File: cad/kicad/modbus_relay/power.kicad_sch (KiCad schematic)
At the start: 18 parts, among them Q6 AO3401A, U3 LMR33630ADDA

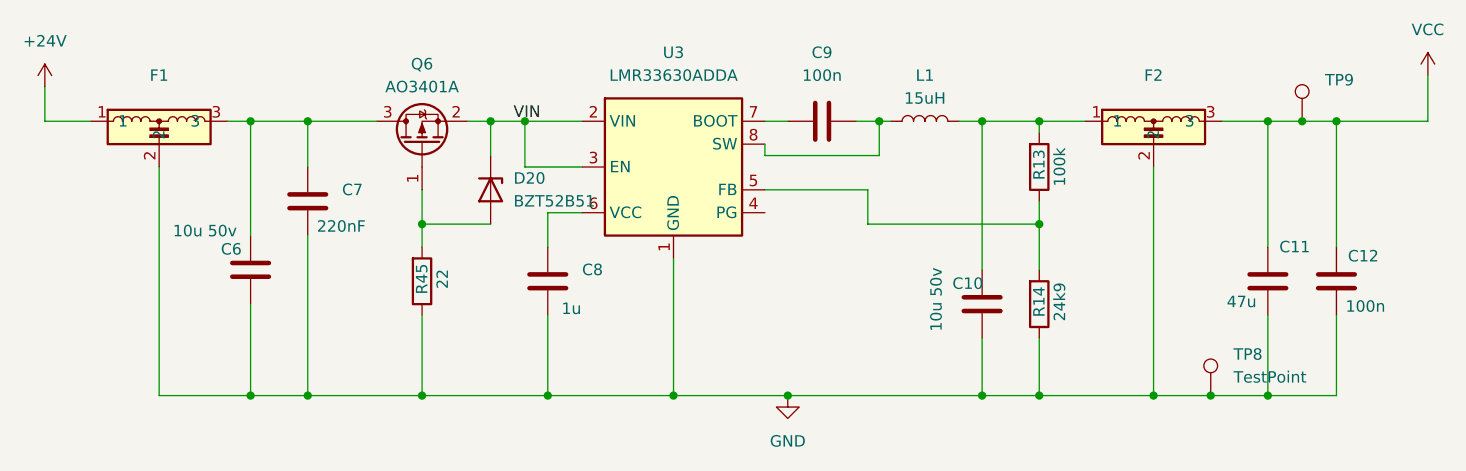
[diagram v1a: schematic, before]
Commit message: Double sided version
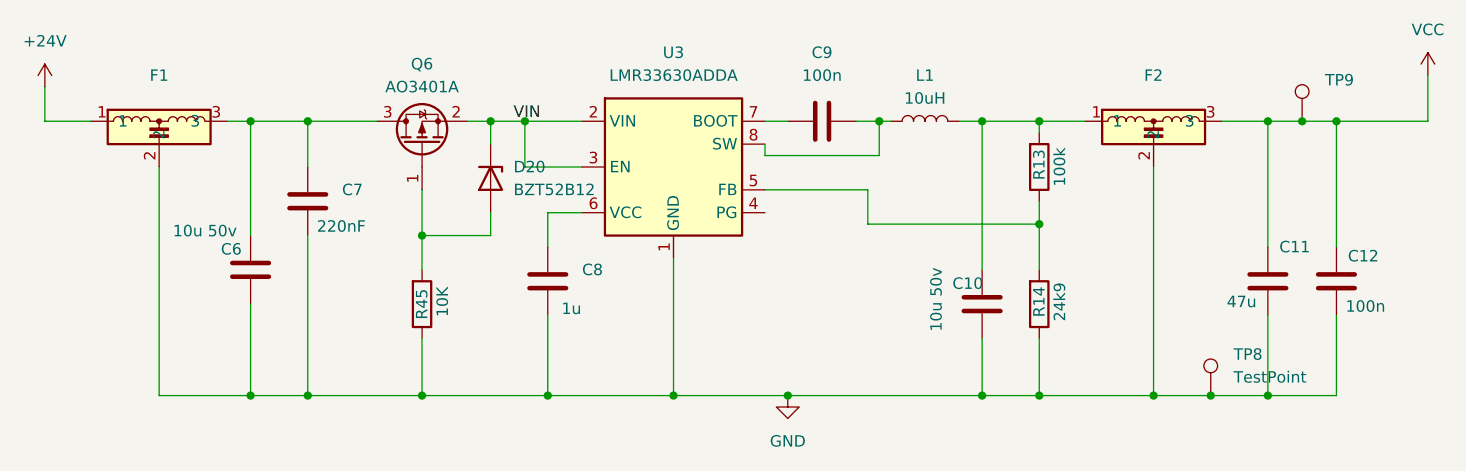
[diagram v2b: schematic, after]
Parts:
- C12: footprint Capacitor_SMD:C_0603_1608Metric_Pad1.08x0.95mm_HandSolder -> Capacitor_SMD:C_0805_2012Metric_Pad1.18x1.45mm_HandSolder
- D20: value BZT52B51 -> BZT52B12
- L1: value 15uH -> 10uH; footprint Inductor_SMD:L_Wuerth_HCM-7070 -> Inductor_SMD:L_Bourns_SRP6060FA
- R13, R14: footprint Resistor_SMD:R_0603_1608Metric_Pad0.98x0.95mm_HandSolder -> Resistor_SMD:R_0805_2012Metric_Pad1.20x1.40mm_HandSolder
- R45: value 22 -> 10K; footprint Resistor_SMD:R_0603_1608Metric_Pad0.98x0.95mm_HandSolder -> Resistor_SMD:R_0805_2012Metric_Pad1.20x1.40mm_HandSolder
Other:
- moved on the sheet: D20, R45
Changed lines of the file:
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@@
-	)
-	(junction
-		(at 107.95 92.71)
-		(diameter 0)
-		(color 0 0 0 0)
 	)
 	(junction
@@
 	)
 	(junction
+		(at 107.95 93.98)
+		(diameter 0)
+		(color 0 0 0 0)
+	)
+	(junction
 		(at 201.93 81.28)
 		(diameter 0)
@@
 	(wire
 		(pts
+			(xy 107.95 88.9) (xy 107.95 93.98)
+		)
+		(stroke
+			(width 0)
+			(type default)
+		)
+	)
+	(wire
+		(pts
 			(xy 125.73 91.44) (xy 121.92 91.44)
 		)
@@
 	(wire
 		(pts
-			(xy 107.95 88.9) (xy 107.95 92.71)
-		)
-		(stroke
-			(width 0)
-			(type default)
-		)
-	)
-	(wire
-		(pts
 			(xy 157.48 88.9) (xy 146.05 88.9)
 		)
@@
 	(wire
 		(pts
-			(xy 107.95 102.87) (xy 107.95 111.76)
+			(xy 107.95 105.41) (xy 107.95 111.76)
 		)
 		(stroke
@@
 	(wire
 		(pts
+			(xy 107.95 93.98) (xy 107.95 97.79)
+		)
+		(stroke
+			(width 0)
+			(type default)
+		)
+	)
+	(wire
+		(pts
 			(xy 95.25 93.98) (xy 95.25 111.76)
 		)
@@
 	(wire
 		(pts
-			(xy 115.57 81.28) (xy 115.57 85.09)
+			(xy 115.57 81.28) (xy 115.57 83.82)
 		)
 		(stroke
@@
 	(wire
 		(pts
-			(xy 107.95 92.71) (xy 115.57 92.71)
-		)
-		(stroke
-			(width 0)
-			(type default)
-		)
-	)
-	(wire
-		(pts
-			(xy 107.95 92.71) (xy 107.95 95.25)
+			(xy 107.95 93.98) (xy 115.57 93.98)
 		)
 		(stroke
@@
 		(pts
 			(xy 176.53 92.71) (xy 176.53 97.79)
+		)
+		(stroke
+			(width 0)
+			(type default)
+		)
+	)
+	(wire
+		(pts
+			(xy 115.57 93.98) (xy 115.57 91.44)
 		)
 		(stroke
@@
 			)
 		)
-		(property "Value" "15uH"
+		(property "Value" "10uH"
 			(at 163.83 78.74 90)
 			(effects
@@
 			)
 		)
-		(property "Footprint" "Inductor_SMD:L_Wuerth_HCM-7070"
+		(property "Footprint" "Inductor_SMD:L_Bourns_SRP6060FA"
 			(at 163.83 81.28 0)
 			(effects
@@
 			)
 		)
-		(property "Footprint" "Resistor_SMD:R_0603_1608Metric_Pad0.98x0.95mm_HandSolder"
+		(property "Footprint" "Resistor_SMD:R_0805_2012Metric_Pad1.20x1.40mm_HandSolder"
 			(at 174.752 101.6 90)
 			(effects
@@
 			)
 		)
-		(property "Footprint" "Capacitor_SMD:C_0603_1608Metric_Pad1.08x0.95mm_HandSolder"
+		(property "Footprint" "Capacitor_SMD:C_0805_2012Metric_Pad1.18x1.45mm_HandSolder"
 			(at 208.5848 95.25 0)
 			(effects
@@
 			)
 		)
-		(property "Footprint" "Resistor_SMD:R_0603_1608Metric_Pad0.98x0.95mm_HandSolder"
+		(property "Footprint" "Resistor_SMD:R_0805_2012Metric_Pad1.20x1.40mm_HandSolder"
 			(at 174.752 86.36 90)
 			(effects
@@
 	(symbol
 		(lib_id "Diode:BZT52Bxx")
-		(at 115.57 88.9 270)
+		(at 115.57 87.63 270)
 		(unit 1)
 		(exclude_from_sim no)
@@
 		(on_board yes)
 		(dnp no)
-		(fields_autoplaced yes)
 		(property "Reference" "D20"
-			(at 118.11 87.6299 90)
+			(at 118.11 86.3599 90)
 			(effects
 				(font
@@
 			)
 		)
-		(property "Value" "BZT52B51"
-			(at 118.11 90.1699 90)
+		(property "Value" "BZT52B12"
+			(at 118.11 88.9 90)
 			(effects
 				(font
@@
 		)
 		(property "Footprint" "Diode_SMD:D_SOD-123F"
-			(at 111.125 88.9 0)
+			(at 111.125 87.63 0)
 			(effects
 				(font
@@
 		)
 		(property "Datasheet" "https://diotec.com/tl_files/diotec/files/pdf/datasheets/bzt52b2v4.pdf"
-			(at 115.57 88.9 0)
+			(at 115.57 87.63 0)
 			(effects
 				(font
@@
 		)
 		(property "Description" "500mW Zener Diode, SOD-123F"
-			(at 115.57 88.9 0)
+			(at 115.57 87.63 0)
 			(effects
 				(font
@@
 	(symbol
 		(lib_id "Device:R")
-		(at 107.95 99.06 0)
+		(at 107.95 101.6 0)
 		(mirror x)
 		(unit 1)
@@
 		(dnp no)
 		(property "Reference" "R45"
-			(at 107.95 98.806 90)
-			(effects
-				(font
-					(size 1.27 1.27)
-				)
-			)
-		)
-		(property "Value" "22"
-			(at 110.236 98.806 90)
-			(effects
-				(font
-					(size 1.27 1.27)
-				)
-			)
-		)
-		(property "Footprint" "Resistor_SMD:R_0603_1608Metric_Pad0.98x0.95mm_HandSolder"
-			(at 106.172 99.06 90)
+			(at 107.95 101.6 90)
+			(effects
+				(font
+					(size 1.27 1.27)
+				)
+			)
+		)
+		(property "Value" "10K"
+			(at 110.236 101.346 90)
+			(effects
+				(font
+					(size 1.27 1.27)
+				)
+			)
+		)
+		(property "Footprint" "Resistor_SMD:R_0805_2012Metric_Pad1.20x1.40mm_HandSolder"
+			(at 106.172 101.6 90)
 			(effects
 				(font
@@
 		)
 		(property "Datasheet" "~"
-			(at 107.95 99.06 0)
+			(at 107.95 101.6 0)
 			(effects
 				(font
@@
 		)
 		(property "Description" "Resistor"
-			(at 107.95 99.06 0)
-			(effects
-				(font
+			(at 107.95 101.6 0)
+			(effects
+				(font
